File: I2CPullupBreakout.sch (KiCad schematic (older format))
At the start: 17 parts, among them J1 SPDT_JUMPER, J2 SPDT_JUMPER, J3 SPDT_JUMPER, J4 SPDT_JUMPER, P1 CONN_6

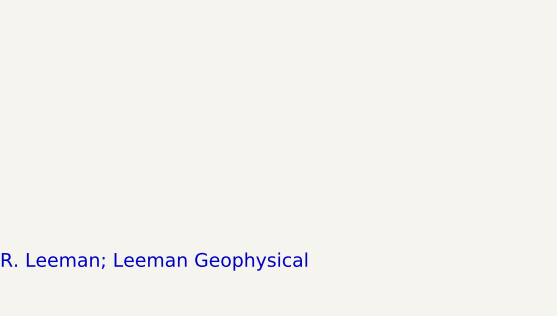
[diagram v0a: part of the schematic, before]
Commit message: Add schematic PDF and rev number.
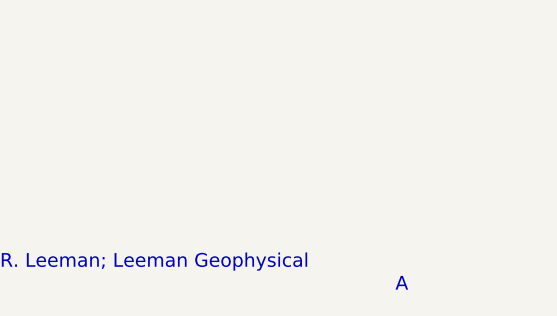
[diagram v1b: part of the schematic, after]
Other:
- note added: "A"
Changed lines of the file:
@@
 LIBS:valves
 LIBS:Jumpers
+LIBS:I2CPullupBreakout-cache
 EELAYER 27 0
 EELAYER END
@@
 Sheet 1 1
 Title ""
-Date "11 nov 2014"
+Date "7 dec 2014"
 Rev ""
 Comp ""
@@
 Wire Wire Line
 	7200 2750 7200 2800
+Text Notes 10600 7650 0    60   ~ 0
+A
 $EndSCHEMATC
